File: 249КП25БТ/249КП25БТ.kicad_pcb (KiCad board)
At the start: 2 copper layers, 15.5 x 13.8 mm, 5 parts

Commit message: добавлены проекты и файлы производства всех плат
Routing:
- net (no net): track 8.60 -> 9.85 mm
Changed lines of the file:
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@@
     (thickness 1.6)
     (drawings 7)
-    (tracks 102)
+    (tracks 106)
     (zones 0)
     (modules 5)
@@
       (drillshape 0)
       (scaleselection 1)
-      (outputdirectory "GERBER/"))
+      (outputdirectory "GERBER/maf_2/"))
   )
   (net 0 "")
@@
   (segment (start 128.230001 70.65) (end 128.33 70.65) (width 0.25) (layer F.Cu) (net 0))
   (segment (start 128.230001 70.65) (end 128.23 71.55) (width 0.25) (layer F.Cu) (net 0))
+  (segment (start 119 67) (end 119 66.5) (width 0.25) (layer F.Cu) (net 0))
+  (segment (start 119 77.75) (end 119 78) (width 0.25) (layer F.Cu) (net 0))
+  (segment (start 119 78) (end 118.75 78) (width 0.25) (layer F.Cu) (net 0))
+  (segment (start 119 78) (end 119.25 78) (width 0.25) (layer F.Cu) (net 0))
   (segment (start 118.8692 68) (end 118.65001 68) (width 0.25) (layer F.Cu) (net 1))
   (segment (start 120.2742 66.595) (end 118.8692 68) (width 0.25) (layer F.Cu) (net 1))

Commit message: Резонит плакал
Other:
- board size 15.5 x 13.8 mm -> 15 x 13.8 mm
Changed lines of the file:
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@@
-(kicad_pcb (version 20171130) (host pcbnew "(5.0.0)")
+(kicad_pcb (version 20171130) (host pcbnew "(5.0.2)-1")
   (general
     (thickness 1.6)
-    (drawings 7)
+    (drawings 6)
     (tracks 106)
     (zones 0)
@@
       (drillshape 0)
       (scaleselection 1)
-      (outputdirectory "GERBER/maf_2/"))
+      (outputdirectory "maf_2/"))
   )
   (net 0 "")
@@
     (effects (font (size 1.5 1.5) (thickness 0.3)) (justify mirror))
   )
-  (gr_line (start 118.25 65.5) (end 118.25 68) (layer Edge.Cuts) (width 0.15))
-  (gr_line (start 133.75 65.5) (end 118.25 65.5) (layer Edge.Cuts) (width 0.15))
-  (gr_line (start 133.75 79.25) (end 133.75 65.5) (layer Edge.Cuts) (width 0.15))
-  (gr_line (start 118.25 79.25) (end 133.75 79.25) (layer Edge.Cuts) (width 0.15))
-  (gr_line (start 118.25 68) (end 118.25 79.25) (layer Edge.Cuts) (width 0.15))
+  (gr_line (start 133.5 65.5) (end 118.5 65.5) (layer Edge.Cuts) (width 0.15))
+  (gr_line (start 133.5 79.25) (end 133.5 65.5) (layer Edge.Cuts) (width 0.15))
+  (gr_line (start 118.5 79.25) (end 133.5 79.25) (layer Edge.Cuts) (width 0.15))
+  (gr_line (start 118.5 65.5) (end 118.5 79.25) (layer Edge.Cuts) (width 0.15))
   (segment (start 121.4 66) (end 121.4 65.90001) (width 0.25) (layer F.Cu) (net 0))
   (segment (start 121.4 65.90001) (end 122.39999 65.90001) (width 0.25) (layer F.Cu) (net 0))

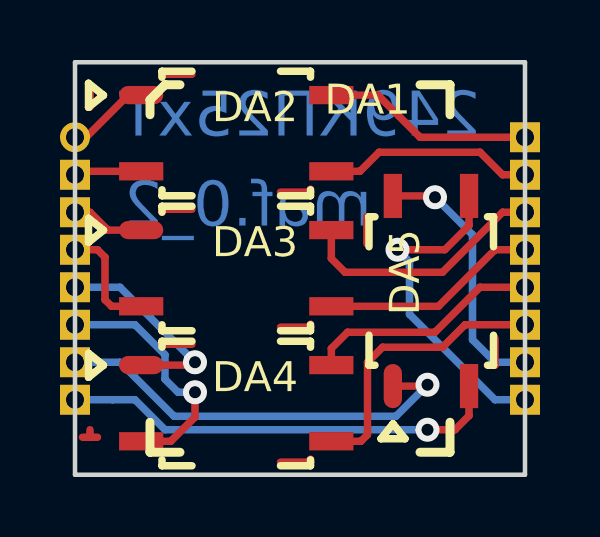
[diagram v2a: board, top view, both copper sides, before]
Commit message: увеличены зазоры и квадратизированы площадки
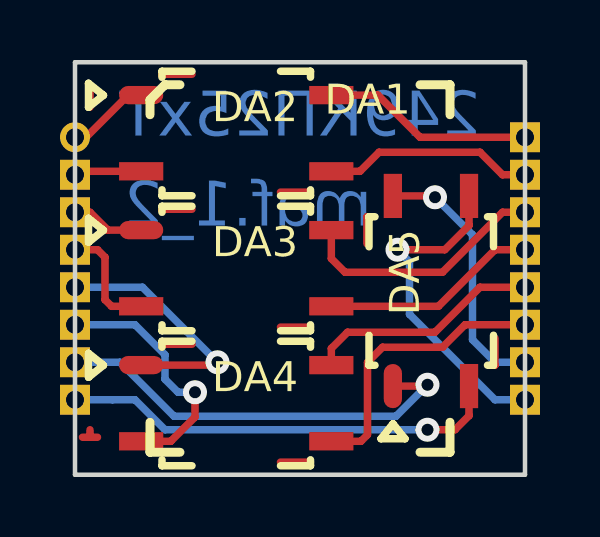
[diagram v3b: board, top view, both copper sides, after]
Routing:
- net /in_3: track 6.87 -> 8.37 mm
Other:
- board text added: "maf.1_2"
- board text removed: "maf.0_2"
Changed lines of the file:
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@@
-(kicad_pcb (version 20171130) (host pcbnew "(5.0.2)-1")
+(kicad_pcb (version 20171130) (host pcbnew "(5.0.0)")
   (general
     (thickness 1.6)
     (drawings 6)
-    (tracks 106)
+    (tracks 103)
     (zones 0)
     (modules 5)
@@
       (drillshape 0)
       (scaleselection 1)
-      (outputdirectory "maf_2/"))
+      (outputdirectory "maf1_2/"))
   )
   (net 0 "")
@@
     )
   )
-  (gr_text maf.0_2 (at 124.25 70.25) (layer B.Cu)
+  (gr_text maf.1_2 (at 124.25 70.25) (layer B.Cu)
     (effects (font (size 1.5 1.5) (thickness 0.3)) (justify mirror))
   )
@@
   (segment (start 121.4 75) (end 121.4 74.90001) (width 0.25) (layer F.Cu) (net 0))
   (segment (start 126.35 78.82999) (end 125.35001 78.82999) (width 0.25) (layer F.Cu) (net 0))
-  (segment (start 126.349999 78.73) (end 126.35 78.82999) (width 0.25) (layer F.Cu) (net 0))
   (segment (start 126.35 74.32999) (end 125.35001 74.32999) (width 0.25) (layer F.Cu) (net 0))
-  (segment (start 126.349999 74.23) (end 126.35 74.32999) (width 0.25) (layer F.Cu) (net 0))
   (segment (start 126.35 69.82999) (end 125.35001 69.82999) (width 0.25) (layer F.Cu) (net 0))
-  (segment (start 126.349999 69.73) (end 126.35 69.82999) (width 0.25) (layer F.Cu) (net 0))
   (segment (start 132.5 75.6) (end 132.4 75.6) (width 0.25) (layer F.Cu) (net 0))
   (segment (start 132.5 75.6) (end 132.5 74.7) (width 0.25) (layer F.Cu) (net 0))
@@
   (segment (start 130.615 73.635) (end 132.5 71.75) (width 0.25) (layer F.Cu) (net 8))
   (segment (start 127.044 73.635) (end 130.615 73.635) (width 0.25) (layer F.Cu) (net 8))
-  (via (at 122.5 75.5) (size 0.8) (drill 0.4) (layers F.Cu B.Cu) (net 9))
-  (segment (start 120.706 75.595) (end 122.405 75.595) (width 0.25) (layer F.Cu) (net 9))
-  (segment (start 122.405 75.595) (end 122.5 75.5) (width 0.25) (layer F.Cu) (net 9))
-  (segment (start 120 73) (end 118.5 73) (width 0.25) (layer B.Cu) (net 9))
-  (segment (start 122.5 75.5) (end 120 73) (width 0.25) (layer B.Cu) (net 9))
+  (via (at 123.25 75.5) (size 0.8) (drill 0.4) (layers F.Cu B.Cu) (net 9))
+  (segment (start 120.75 73) (end 123.25 75.5) (width 0.25) (layer B.Cu) (net 9))
+  (segment (start 118.5 73) (end 120.75 73) (width 0.25) (layer B.Cu) (net 9))
+  (segment (start 123.155 75.595) (end 123.25 75.5) (width 0.25) (layer F.Cu) (net 9))
+  (segment (start 120.706 75.595) (end 123.155 75.595) (width 0.25) (layer F.Cu) (net 9))
   (segment (start 127.044 75.0402) (end 127.5842 74.5) (width 0.25) (layer F.Cu) (net 10))
   (segment (start 127.044 75.595) (end 127.044 75.0402) (width 0.25) (layer F.Cu) (net 10))
